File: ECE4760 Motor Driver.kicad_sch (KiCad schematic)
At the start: 61 parts, among them J1 IO, J100 Alternative Motor, J2 Motor / Power, J3 USB_B_Micro, J4 UART, J5 Debug, J6 Boot, U1 STM32G473V_B-C-E_Hx, U5 TLV75733PDBV, X1 48MHz

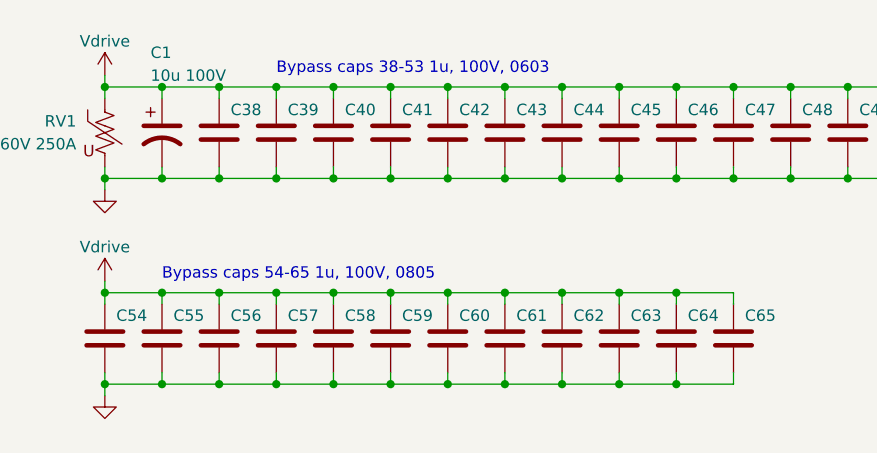
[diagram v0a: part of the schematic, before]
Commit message: Updating cap specs
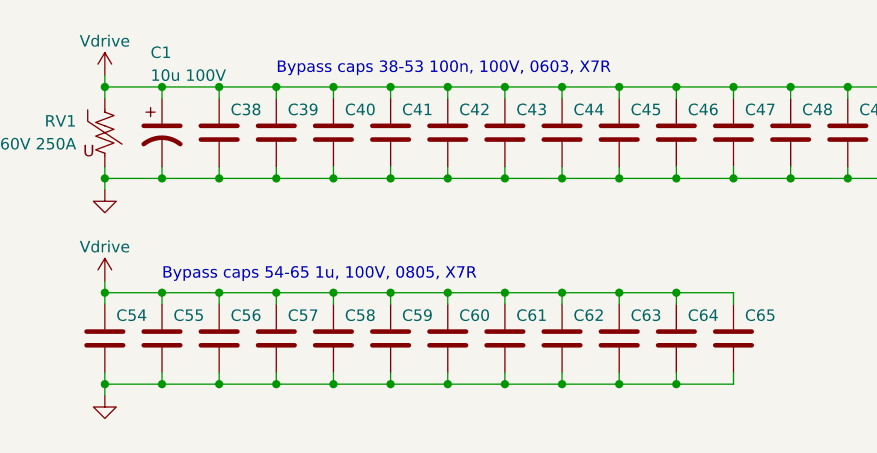
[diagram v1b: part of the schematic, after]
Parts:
- C38, C39, C40, C41, C42, C43, C44, C45, C46, C47, C48, C49, C50, C51, C52, C53: value 1u, 100V -> 100n, 100V
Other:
- note added: "Bypass caps 38-53 100n, 100V, 0603, X7R"
- note added: "Bypass caps 54-65 1u, 100V, 0805, X7R"
- note removed: "Bypass caps 38-53 1u, 100V, 0603"
- note removed: "Bypass caps 54-65 1u, 100V, 0805"
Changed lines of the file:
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@@
     (effects (font (size 1.27 1.27)) (justify left bottom))
   )
-  (text "Bypass caps 38-53 1u, 100V, 0603" (at 171.45 19.05 0)
+  (text "Bypass caps 38-53 100n, 100V, 0603, X7R" (at 171.45 19.05 0)
     (effects (font (size 1.27 1.27)) (justify left bottom))
   )
@@
     (effects (font (size 1.27 1.27) (color 194 0 0 1)) (justify left bottom))
   )
-  (text "Bypass caps 54-65 1u, 100V, 0805" (at 158.75 41.91 0)
+  (text "Bypass caps 54-65 1u, 100V, 0805, X7R" (at 158.75 41.91 0)
     (effects (font (size 1.27 1.27)) (justify left bottom))
   )
@@
       (effects (font (size 1.27 1.27)) (justify left))
     )
-    (property "Value" "1u, 100V" (at 242.57 27.94 0)
+    (property "Value" "100n, 100V" (at 242.57 27.94 0)
       (effects (font (size 1.27 1.27)) (justify left) hide)
     )
@@
       (effects (font (size 1.27 1.27)) (justify left))
     )
-    (property "Value" "1u, 100V" (at 223.52 27.94 0)
+    (property "Value" "100n, 100V" (at 223.52 27.94 0)
       (effects (font (size 1.27 1.27)) (justify left) hide)
     )
@@
       (effects (font (size 1.27 1.27)) (justify left))
     )
-    (property "Value" "1u, 100V" (at 179.07 27.94 0)
+    (property "Value" "100n, 100V" (at 179.07 27.94 0)
       (effects (font (size 1.27 1.27)) (justify left) hide)
     )
@@
       (effects (font (size 1.27 1.27)) (justify left))
     )
-    (property "Value" "1u, 100V" (at 204.47 27.94 0)
+    (property "Value" "100n, 100V" (at 204.47 27.94 0)
       (effects (font (size 1.27 1.27)) (justify left) hide)
     )
@@
       (effects (font (size 1.27 1.27)) (justify left))
     )
-    (property "Value" "1u, 100V" (at 210.82 27.94 0)
+    (property "Value" "100n, 100V" (at 210.82 27.94 0)
       (effects (font (size 1.27 1.27)) (justify left) hide)
     )
@@
       (effects (font (size 1.27 1.27)) (justify left))
     )
-    (property "Value" "1u, 100V" (at 261.62 27.94 0)
+    (property "Value" "100n, 100V" (at 261.62 27.94 0)
       (effects (font (size 1.27 1.27)) (justify left) hide)
     )
@@
       (effects (font (size 1.27 1.27)) (justify left))
     )
-    (property "Value" "1u, 100V" (at 191.77 27.94 0)
+    (property "Value" "100n, 100V" (at 191.77 27.94 0)
       (effects (font (size 1.27 1.27)) (justify left) hide)
     )
@@
       (effects (font (size 1.27 1.27)) (justify left))
     )
-    (property "Value" "1u, 100V" (at 172.72 27.94 0)
+    (property "Value" "100n, 100V" (at 172.72 27.94 0)
       (effects (font (size 1.27 1.27)) (justify left) hide)
     )
@@
       (effects (font (size 1.27 1.27)) (justify left))
     )
-    (property "Value" "1u, 100V" (at 166.37 27.94 0)
+    (property "Value" "100n, 100V" (at 166.37 27.94 0)
       (effects (font (size 1.27 1.27)) (justify left) hide)
     )
@@
       (effects (font (size 1.27 1.27)) (justify left))
     )
-    (property "Value" "1u, 100V" (at 248.92 27.94 0)
+    (property "Value" "100n, 100V" (at 248.92 27.94 0)
       (effects (font (size 1.27 1.27)) (justify left) hide)
     )
@@
       (effects (font (size 1.27 1.27)) (justify left))
     )
-    (property "Value" "1u, 100V" (at 217.17 27.94 0)
+    (property "Value" "100n, 100V" (at 217.17 27.94 0)
       (effects (font (size 1.27 1.27)) (justify left) hide)
     )
@@
       (effects (font (size 1.27 1.27)) (justify left))
     )
-    (property "Value" "1u, 100V" (at 185.42 27.94 0)
+    (property "Value" "100n, 100V" (at 185.42 27.94 0)
       (effects (font (size 1.27 1.27)) (justify left) hide)
     )
@@
       (effects (font (size 1.27 1.27)) (justify left))
     )
-    (property "Value" "1u, 100V" (at 198.12 27.94 0)
+    (property "Value" "100n, 100V" (at 198.12 27.94 0)
       (effects (font (size 1.27 1.27)) (justify left) hide)
     )
@@
       (effects (font (size 1.27 1.27)) (justify left))
     )
-    (property "Value" "1u, 100V" (at 229.87 27.94 0)
+    (property "Value" "100n, 100V" (at 229.87 27.94 0)
       (effects (font (size 1.27 1.27)) (justify left) hide)
     )
@@
       (effects (font (size 1.27 1.27)) (justify left))
     )
-    (property "Value" "1u, 100V" (at 236.22 27.94 0)
+    (property "Value" "100n, 100V" (at 236.22 27.94 0)
       (effects (font (size 1.27 1.27)) (justify left) hide)
     )
@@
       (effects (font (size 1.27 1.27)) (justify left))
     )
-    (property "Value" "1u, 100V" (at 255.27 27.94 0)
+    (property "Value" "100n, 100V" (at 255.27 27.94 0)
       (effects (font (size 1.27 1.27)) (justify left) hide)
     )

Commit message: Getting ready for fab
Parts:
- removed C38, C39, C40, C41, C42, C43, C44, C45, C46, C47, C48, C49, C50, C51, C52, C53: 100n, 100V, Capacitor_SMD:C_0603_1608Metric, symbol Device:C
- removed C54, C55, C56, C57, C58, C59, C60, C61, C62, C63, C64, C65: 1u, 100V, Capacitor_SMD:C_0805_2012Metric, symbol Device:C
- added TP1: TestPoint, TestPoint:TestPoint_Pad_D2.0mm, symbol Connector:TestPoint
- C10, C11, C3, C6, C7, C8, C9: DigiKey (none) -> 490-10700-1-ND
- H1, H2, H3, H4: now left out of the parts list
- R1: DigiKey (none) -> 311-1.00KLRCT-ND
- R2, R3: value 5k -> 1k; DigiKey (none) -> 311-1.00KLRCT-ND
- U5: LCSC (none) -> C485517
- X1: LCSC (none) -> C3034286
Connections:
- net GND: now also TP1.1
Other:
- note removed: "Bypass caps 38-53 100n, 100V, 0603, X7R"
- note removed: "Bypass caps 54-65 1u, 100V, 0805, X7R"
- moved on the sheet: C1, RV1

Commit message: Single-sided component placement
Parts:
- removed J6: Boot, Connector_PinHeader_2.54mm:PinHeader_1x02_P2.54mm_Vertical, symbol Connector_Generic:Conn_01x02
- added C74: 100n, 100V, 0603, X7R, Capacitor_SMD:C_0603_1608Metric, symbol Device:C
- added C75: 1u, 100V, 0805, X7R, Capacitor_SMD:C_0805_2012Metric, symbol Device:C
- added C76: 1u, Capacitor_SMD:C_0603_1608Metric, symbol Device:C
- added C77, C78: 22u, Capacitor_SMD:C_0805_2012Metric, symbol Device:C
- added C79, C80, C81: 100n, Capacitor_SMD:C_0402_1005Metric, symbol Device:C
- added D2: LED, LED_SMD:LED_1206_3216Metric, symbol Device:LED
- added R43, R45: 10k, Resistor_SMD:R_0402_1005Metric, symbol Device:R_US
- added R44: 40k2, Resistor_SMD:R_0402_1005Metric, symbol Device:R_US
- added SW1: BOOT, Button_Switch_SMD:SW_SPST_PTS810, symbol Switch:SW_Push
- added U7: TPSM365R6, TPSM:RDN0011A-MFG, symbol TPSM:TPSM365R6FRDNR
- C12, C13: value 1u -> 4u7; footprint Capacitor_SMD:C_0805_2012Metric -> Capacitor_SMD:C_0603_1608Metric
- J1: footprint Connector_PinSocket_2.54mm:PinSocket_2x17_P2.54mm_Vertical -> Connector_PinSocket_2.54mm:PinSocket_2x20_P2.54mm_Vertical; symbol Connector_Generic:Conn_02x17_Odd_Even -> Connector_Generic:Conn_02x20_Odd_Even
- J100: footprint Connector_PinSocket_2.54mm:PinSocket_2x14_P2.54mm_Vertical -> Connector_PinSocket_2.54mm:PinSocket_2x12_P2.54mm_Vertical; symbol Connector_Generic:Conn_02x14_Odd_Even -> Connector_Generic:Conn_02x12_Odd_Even
- J2: footprint Connector_Phoenix_MC_HighVoltage:PhoenixContact_MCV_1,5_7-G-5.08_1x07_P5.08mm_Vertical -> Connector_Phoenix_MC_HighVoltage:PhoenixContact_MCV_1,5_6-G-5.08_1x06_P5.08mm_Vertical; symbol Connector:Screw_Terminal_01x07 -> Connector:Screw_Terminal_01x06
- J4, J5: LCSC (none) -> C514175
- RV1: LCSC (none) -> C2760142
- TP1: now left out of the parts list
- U5: value TLV75733PDBV -> AP7361C-33FGE; footprint Package_TO_SOT_SMD:SOT-23-5 -> Package_DFN_QFN:DFN-8-1EP_3x3mm_P0.5mm_EP1.65x2.38mm; DigiKey 296-50414-1-ND -> AP7361C-33FGE-7DICT-ND; LCSC C485517 -> C151007
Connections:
- net +3V3: now also J1.19 (Pin_19), U5.1 (OUT), C79.1, C80.1, C81.1; no longer J1.20 (Pin_20), U1.F1 (PC2), U1.F4 (PC1), U5.5 (OUT)
- net +5V: now also J1.1 (Pin_1), J1.13 (Pin_13), J1.27 (Pin_27), J1.33 (Pin_33), J1.7 (Pin_7), U5.8 (IN), C77.1, C78.1, R43.1, R44.1, U7.4 (VOUT); no longer J1.14 (Pin_14), J1.2 (Pin_2), J1.28 (Pin_28), J1.34 (Pin_34), J1.8 (Pin_8), J100.25 (Pin_25), J100.26 (Pin_26), J100.27 (Pin_27), J100.28 (Pin_28), J2.7 (Pin_7), U5.1 (IN)
- net Aux_Enc_A_In+: now also J1.11 (Pin_11); no longer J1.12 (Pin_12)
- net Aux_Enc_A_In-: now also J1.12 (Pin_12); no longer J1.11 (Pin_11)
- net Aux_Enc_B_In+: now also J1.9 (Pin_9); no longer J1.10 (Pin_10)
- net Aux_Enc_B_In-: now also J1.10 (Pin_10); no longer J1.9 (Pin_9)
- net BOOT_SELECT: now also SW1.2
- net Enc_A_In+: now also J1.22 (Pin_22); no longer J1.21 (Pin_21)
- net Enc_A_In-: now also J1.21 (Pin_21); no longer J1.22 (Pin_22)
- net Enc_B_In+: now also J1.24 (Pin_24); no longer J1.23 (Pin_23)
- net Enc_B_In-: now also J1.23 (Pin_23); no longer J1.24 (Pin_24)
- net Enc_I_In+: now also J1.26 (Pin_26); no longer J1.25 (Pin_25)
- net Enc_I_In-: now also J1.25 (Pin_25); no longer J1.26 (Pin_26)
- net GND: now also J1.14 (Pin_14), J1.2 (Pin_2), J1.20 (Pin_20), J1.28 (Pin_28), J1.34 (Pin_34), J1.8 (Pin_8), J100.5 (Pin_5), J100.6 (Pin_6), J100.7 (Pin_7), J100.8 (Pin_8), J2.2 (Pin_2), U5.4 (GND), U5.9 (GND), C74.2, C75.2, C76.2, C77.2, C78.2, C79.2, C80.2, C81.2, R45.2, SW1.1, U7.10 (GND); no longer J1.1 (Pin_1), J1.13 (Pin_13), J1.19 (Pin_19), J1.27 (Pin_27), J1.33 (Pin_33), J1.7 (Pin_7), J100.17 (Pin_17), J100.18 (Pin_18), J100.19 (Pin_19), J100.20 (Pin_20), J2.5 (Pin_5), U1.E4 (PF10), U1.G3 (PF2), U1.H5 (PE8), U5.2 (GND)
- net Hall_A_In: now also J1.5 (Pin_5); no longer J1.6 (Pin_6)
- net Hall_B_In: now also J1.3 (Pin_3); no longer J1.4 (Pin_4)
- net Hall_C_In: now also J1.4 (Pin_4); no longer J1.3 (Pin_3)
- net Hall_I_In: now also J1.6 (Pin_6); no longer J1.5 (Pin_5)
- net LED_1: now also J1.18 (Pin_18); no longer J1.17 (Pin_17)
- net LED_2: now also J1.17 (Pin_17); no longer J1.18 (Pin_18)
- net Lim_Aux_In: now also J1.31 (Pin_31); no longer J1.32 (Pin_32)
- net Lim_H_In: now also J1.29 (Pin_29); no longer J1.30 (Pin_30)
- net Lim_L_In: now also J1.30 (Pin_30); no longer J1.29 (Pin_29)
- net Lim_R_In: now also J1.32 (Pin_32); no longer J1.31 (Pin_31)
- net PH1: now also J100.10 (Pin_10), J100.11 (Pin_11), J100.12 (Pin_12), J100.9 (Pin_9), J2.3 (Pin_3); no longer J100.1 (Pin_1), J100.2 (Pin_2), J100.3 (Pin_3), J100.4 (Pin_4), J2.1 (Pin_1)
- net PH2: now also J100.13 (Pin_13), J100.14 (Pin_14), J100.15 (Pin_15), J100.16 (Pin_16), J2.4 (Pin_4); no longer J100.5 (Pin_5), J100.6 (Pin_6), J100.7 (Pin_7), J100.8 (Pin_8), J2.2 (Pin_2)
- net PH3: now also J100.17 (Pin_17), J100.18 (Pin_18), J100.19 (Pin_19), J100.20 (Pin_20), J2.5 (Pin_5); no longer J100.10 (Pin_10), J100.11 (Pin_11), J100.12 (Pin_12), J100.9 (Pin_9), J2.3 (Pin_3)
- net PH4: now also J100.21 (Pin_21), J100.22 (Pin_22), J100.23 (Pin_23), J100.24 (Pin_24), J2.6 (Pin_6); no longer J100.13 (Pin_13), J100.14 (Pin_14), J100.15 (Pin_15), J100.16 (Pin_16), J2.4 (Pin_4)
- net Vdrive: now also J100.1 (Pin_1), J100.2 (Pin_2), J100.3 (Pin_3), J100.4 (Pin_4), J2.1 (Pin_1), C74.1, C75.1, U7.2 (EN), U7.3 (VIN); no longer J100.21 (Pin_21), J100.22 (Pin_22), J100.23 (Pin_23), J100.24 (Pin_24), J2.6 (Pin_6)
- net ~{Abort}: now also J1.16 (Pin_16); no longer J1.15 (Pin_15)
- net ~{Fault_Enable}: now also J1.15 (Pin_15); no longer J1.16 (Pin_16)
- net at U5.3 (NC): now also U5.2 (NC), U5.6 (NC), U5.7 (NC)
- new net: R43.2, U5.5 (EN), U7.1 (PGOOD)
- new net: C76.1, U7.11 (RT), U7.8 (VCC)
- new net: U7.5 (SW), U7.6 (SW)
- new net: R44.2, R45.1, U7.9 (FB)
- no-connect marks 26 -> 31
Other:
- moved on the sheet: C1, C12, C13, RV1, U5

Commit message: Updated routing
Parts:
- F1: DigiKey 283-PTSLR06038V100CT-ND -> MF-FSMF050X-2CT-ND; LCSC (none) -> C210357
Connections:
- net AUX_ENC_A+: no longer U1.J3 (PC5), U1.K3 (PB1)
- net AUX_ENC_A-: no longer U1.K2 (PC4)
- net ENC_A-: no longer U1.K8 (PB12)
- net ENC_I+: no longer U1.F10 (PC7), U1.G9 (PD13)
- net HALL_A: no longer U1.A5 (PB3), U1.B5 (PB5)
- net HALL_C: no longer U1.A6 (PD6)
- net Hall_A_In: now also J1.31 (Pin_31); no longer J1.5 (Pin_5)
- net Hall_B_In: now also J1.29 (Pin_29); no longer J1.3 (Pin_3)
- net Hall_C_In: now also J1.30 (Pin_30); no longer J1.4 (Pin_4)
- net Hall_I_In: now also J1.32 (Pin_32); no longer J1.6 (Pin_6)
- net LIM_AUX: no longer U1.C8 (PC10)
- net LIM_H: no longer U1.E10 (PA8)
- net LIM_L: no longer U1.F9 (PC6)
- net LIM_R: no longer U1.E9 (PC9)
- net Lim_Aux_In: now also J1.5 (Pin_5); no longer J1.31 (Pin_31)
- net Lim_H_In: now also J1.3 (Pin_3); no longer J1.29 (Pin_29)
- net Lim_L_In: now also J1.4 (Pin_4); no longer J1.30 (Pin_30)
- net Lim_R_In: now also J1.6 (Pin_6); no longer J1.32 (Pin_32)
- net PH3_HI: now also U1.A9 (PD1), U1.B9 (PA15)
- net UART_RX: now also U1.A7 (PD5)
- no-connect marks 31 -> 41

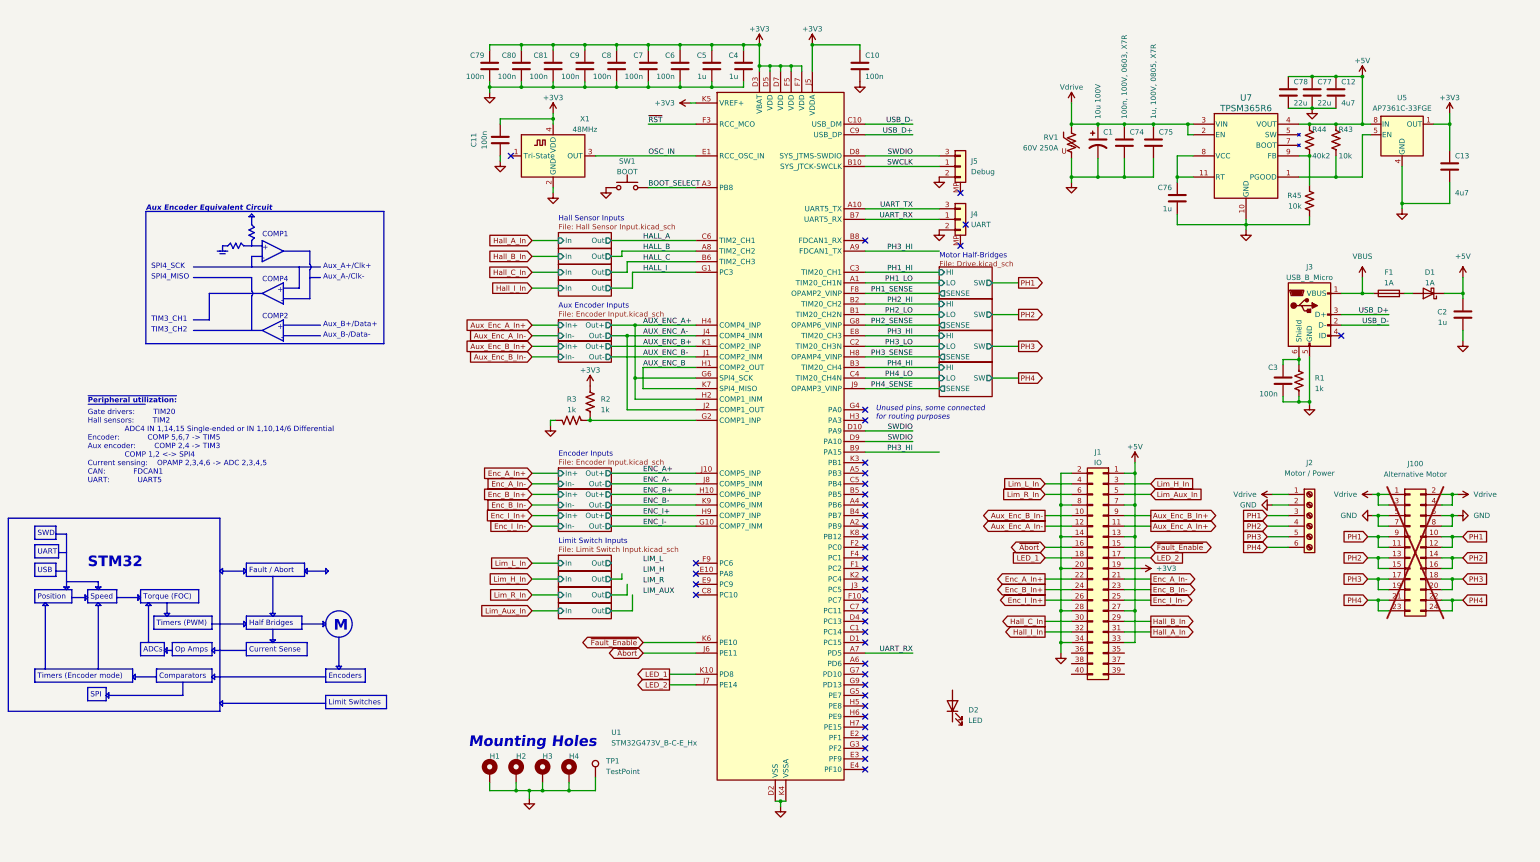
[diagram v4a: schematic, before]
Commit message: Power supply and remove USB
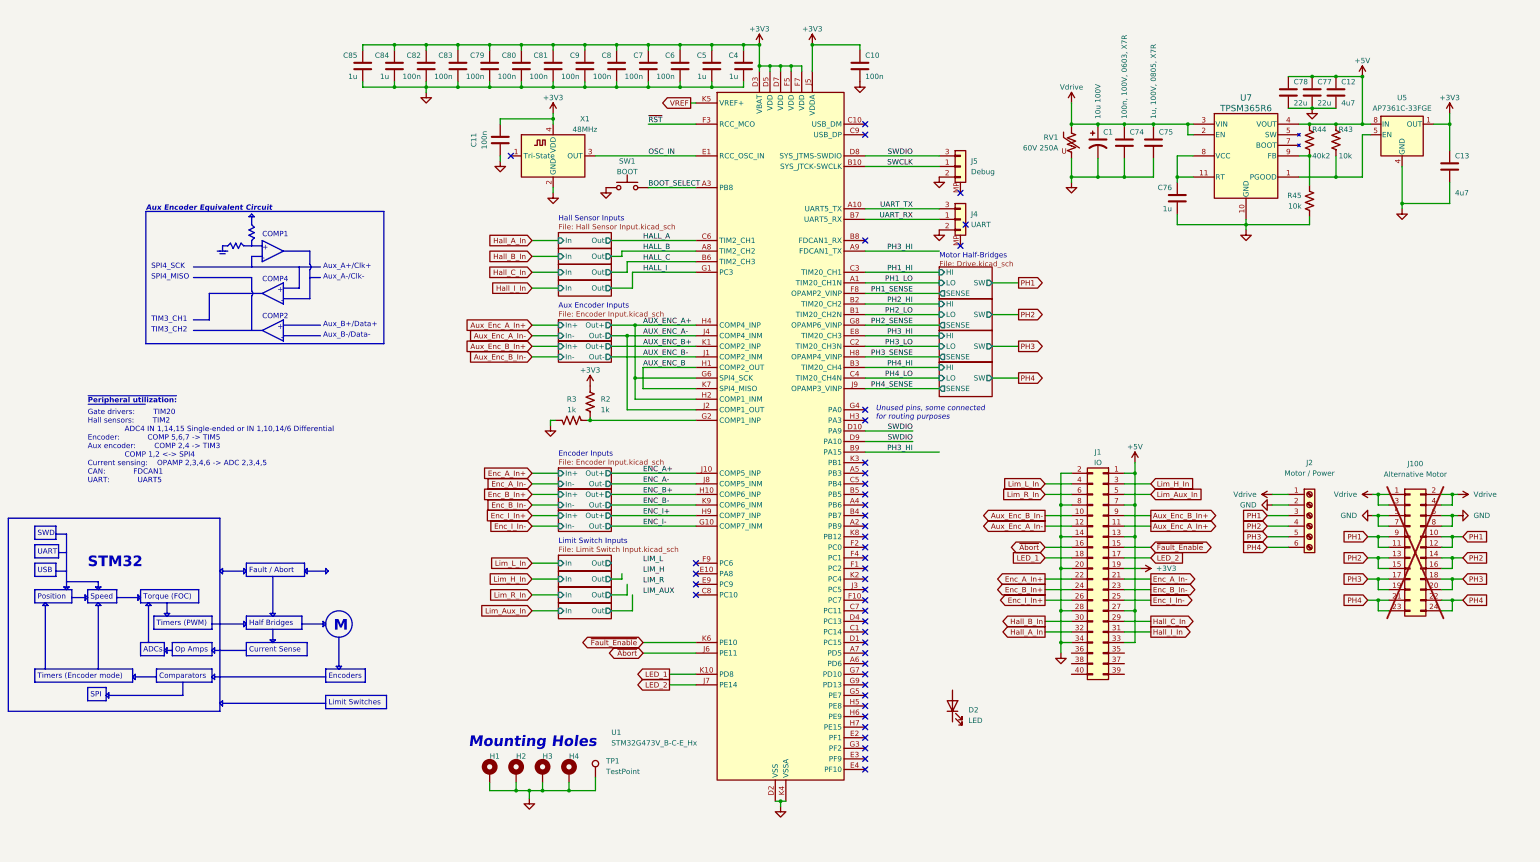
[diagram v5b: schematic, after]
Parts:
- removed C2: 1u, Capacitor_SMD:C_0603_1608Metric, symbol Device:C
- removed C3: 100n, Capacitor_SMD:C_0402_1005Metric, symbol Device:C
- removed D1: 1A, Diode_SMD:D_SOD-323, symbol Device:D_Schottky
- removed F1: 1A, Fuse:Fuse_0603_1608Metric, symbol Device:Fuse
- removed J3: USB_B_Micro, Connector_USB:USB_Micro-B_Molex_47346-0001, symbol Connector:USB_B_Micro
- removed R1: 1k, Resistor_SMD:R_0402_1005Metric, symbol Device:R_US
- added C82, C83: 100n, Capacitor_SMD:C_0402_1005Metric, symbol Device:C
- added C84, C85: 1u, Capacitor_SMD:C_0603_1608Metric, symbol Device:C
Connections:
- net +3V3: now also C82.1, C83.1, C84.1, C85.1; no longer U1.K5 (VREF+)
- net GND: now also C82.2, C83.2, C84.2, C85.2
- net Hall_A_In: now also J1.32 (Pin_32); no longer J1.31 (Pin_31)
- net Hall_B_In: now also J1.30 (Pin_30); no longer J1.29 (Pin_29)
- net Hall_C_In: now also J1.29 (Pin_29); no longer J1.30 (Pin_30)
- net Hall_I_In: now also J1.31 (Pin_31); no longer J1.32 (Pin_32)
- net UART_RX: no longer U1.A7 (PD5)
- net USB_D+: no longer names the net of U1.C9 (PA12)
- net USB_D-: no longer names the net of U1.C10 (PA11)
- new net VREF: U1.K5 (VREF+)
- no-connect marks 41 -> 43
